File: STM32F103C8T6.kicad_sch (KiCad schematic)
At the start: 23 parts, among them SW1 PTS810, U3 MCU_STM32F103C8Tx, Y1 16MHz

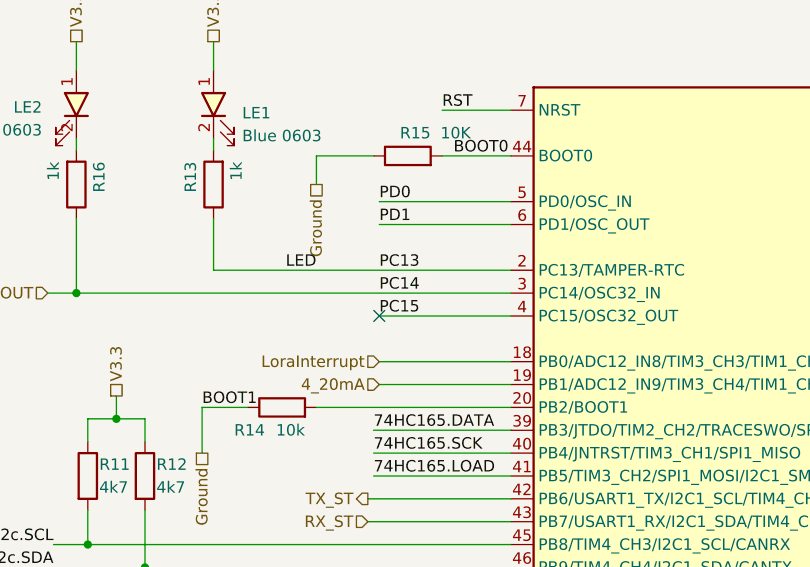
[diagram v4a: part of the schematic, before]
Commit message: Layout p2, fix Analog VCC and GND for opamp circuit
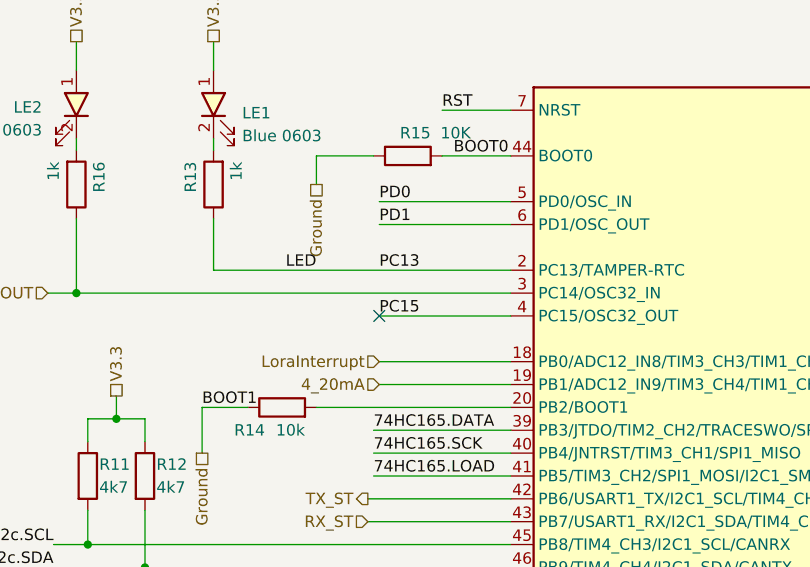
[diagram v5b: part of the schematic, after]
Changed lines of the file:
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@@
-		)
-	)
-	(label "PC14"
-		(at 97.79 107.95 0)
-		(fields_autoplaced yes)
-		(effects
-			(font
-				(size 1.27 1.27)
-			)
-			(justify left bottom)
 		)
 	)

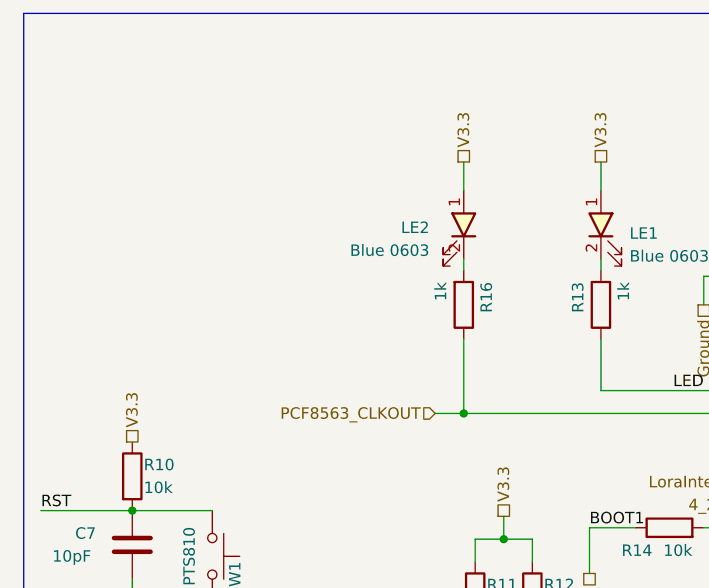
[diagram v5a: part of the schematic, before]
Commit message: feat: Add pullup resistor PCF8563_CLKOUT pin
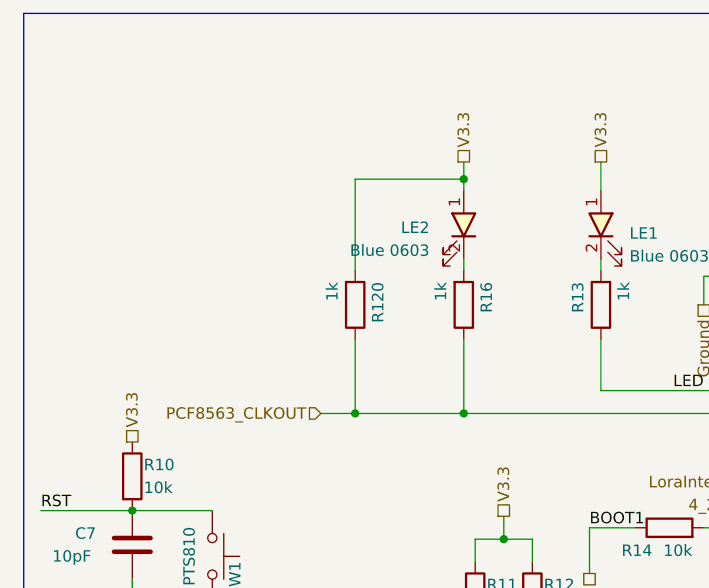
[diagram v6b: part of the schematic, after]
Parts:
- added R120: 1k, SpiritBoi_Footprint_Library:R_0603, symbol Thu_vien_kicad:R
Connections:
- net PCF8563_CLKOUT: now also R120.1
- net V3.3: now also R120.2
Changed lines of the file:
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@@
 	)
 	(junction
+		(at 52.07 107.95)
+		(diameter 0)
+		(color 0 0 0 0)
+	)
+	(junction
 		(at 255.905 138.43)
 		(diameter 0)
@@
 	)
 	(junction
+		(at 64.135 81.915)
+		(diameter 0)
+		(color 0 0 0 0)
+	)
+	(junction
 		(at 98.425 38.1)
 		(diameter 0)
@@
 		)
 	)
+	(wire
+		(pts
+			(xy 52.07 99.695) (xy 52.07 107.95)
+		)
+		(stroke
+			(width 0)
+			(type default)
+		)
+	)
 	(polyline
 		(pts
@@
 	(wire
 		(pts
+			(xy 64.135 81.915) (xy 64.135 83.185)
+		)
+		(stroke
+			(width 0)
+			(type default)
+		)
+	)
+	(wire
+		(pts
 			(xy 308.61 53.34) (xy 316.23 53.34)
 		)
@@
 	(wire
 		(pts
+			(xy 52.07 107.95) (xy 64.135 107.95)
+		)
+		(stroke
+			(width 0)
+			(type default)
+		)
+	)
+	(wire
+		(pts
 			(xy 39.37 45.085) (xy 39.37 47.625)
 		)
@@
 	(wire
 		(pts
-			(xy 60.96 107.95) (xy 64.135 107.95)
+			(xy 48.26 107.95) (xy 52.07 107.95)
 		)
 		(stroke
@@
 	(wire
 		(pts
+			(xy 52.07 92.075) (xy 52.07 81.915)
+		)
+		(stroke
+			(width 0)
+			(type default)
+		)
+	)
+	(wire
+		(pts
 			(xy 93.345 140.97) (xy 112.395 140.97)
 		)
@@
 	(wire
 		(pts
-			(xy 64.135 80.01) (xy 64.135 83.185)
+			(xy 64.135 80.01) (xy 64.135 81.915)
 		)
 		(stroke
@@
 		)
 	)
+	(wire
+		(pts
+			(xy 52.07 81.915) (xy 64.135 81.915)
+		)
+		(stroke
+			(width 0)
+			(type default)
+		)
+	)
 	(bus
 		(pts
@@
 	(hierarchical_label "PCF8563_CLKOUT"
 		(shape input)
-		(at 60.96 107.95 180)
+		(at 48.26 107.95 180)
 		(fields_autoplaced yes)
 		(effects
@@
 					(unit 1)
 				)
+			)
+		)
+	)
+	(symbol
+		(lib_id "Thu_vien_kicad:R")
+		(at 52.07 95.885 0)
+		(mirror x)
+		(unit 1)
+		(exclude_from_sim no)
+		(in_bom yes)
+		(on_board yes)
+		(dnp no)
+		(property "Reference" "R120"
+			(at 54.61 93.345 90)
+			(effects
+				(font
+					(size 1.27 1.27)
+				)
+				(justify left)
+			)
+		)
+		(property "Value" "1k"
+			(at 49.53 93.345 90)
+			(effects
+				(font
+					(size 1.27 1.27)
+				)
+				(justify left)
+			)
+		)
+		(property "Footprint" "SpiritBoi_Footprint_Library:R_0603"
+			(at 50.292 95.885 90)
+			(effects
+				(font
+					(size 1.27 1.27)
+				)
+				(hide yes)
+			)
+		)
+		(property "Datasheet" "~"
+			(at 52.07 95.885 0)
+			(effects
+				(font
+					(size 1.27 1.27)
+				)
+				(hide yes)
+			)
+		)
+		(property "Description" ""
+			(at 52.07 95.885 0)
+			(effects
+				(font
+					(size 1.27 1.27)
+				)
+				(hide yes)
+			)
+		)
+		(pin "1"
+		)
+		(pin "2"
+		)
+		(instances
+			(project "DongTamV2"
+				(path "/2303d546-b88a-4ab0-aee1-26e3b32ac9d7/de1d919d-cc07-489f-afed-971dd930ed54"
+					(reference "R120")
+					(unit 1)
+				)
